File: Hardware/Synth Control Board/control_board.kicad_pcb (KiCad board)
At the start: 2 copper layers, 127 x 177.8 mm, 59 parts, among them J1 Conn_01x13, J10 Conn_01x05, J11 Conn_01x08, J12 Conn_01x06, J2 Conn_01x03, J3 Conn_01x13, J4 Conn_01x13, J5 Conn_01x02, J6 Conn_01x13, J7 Conn_01x05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

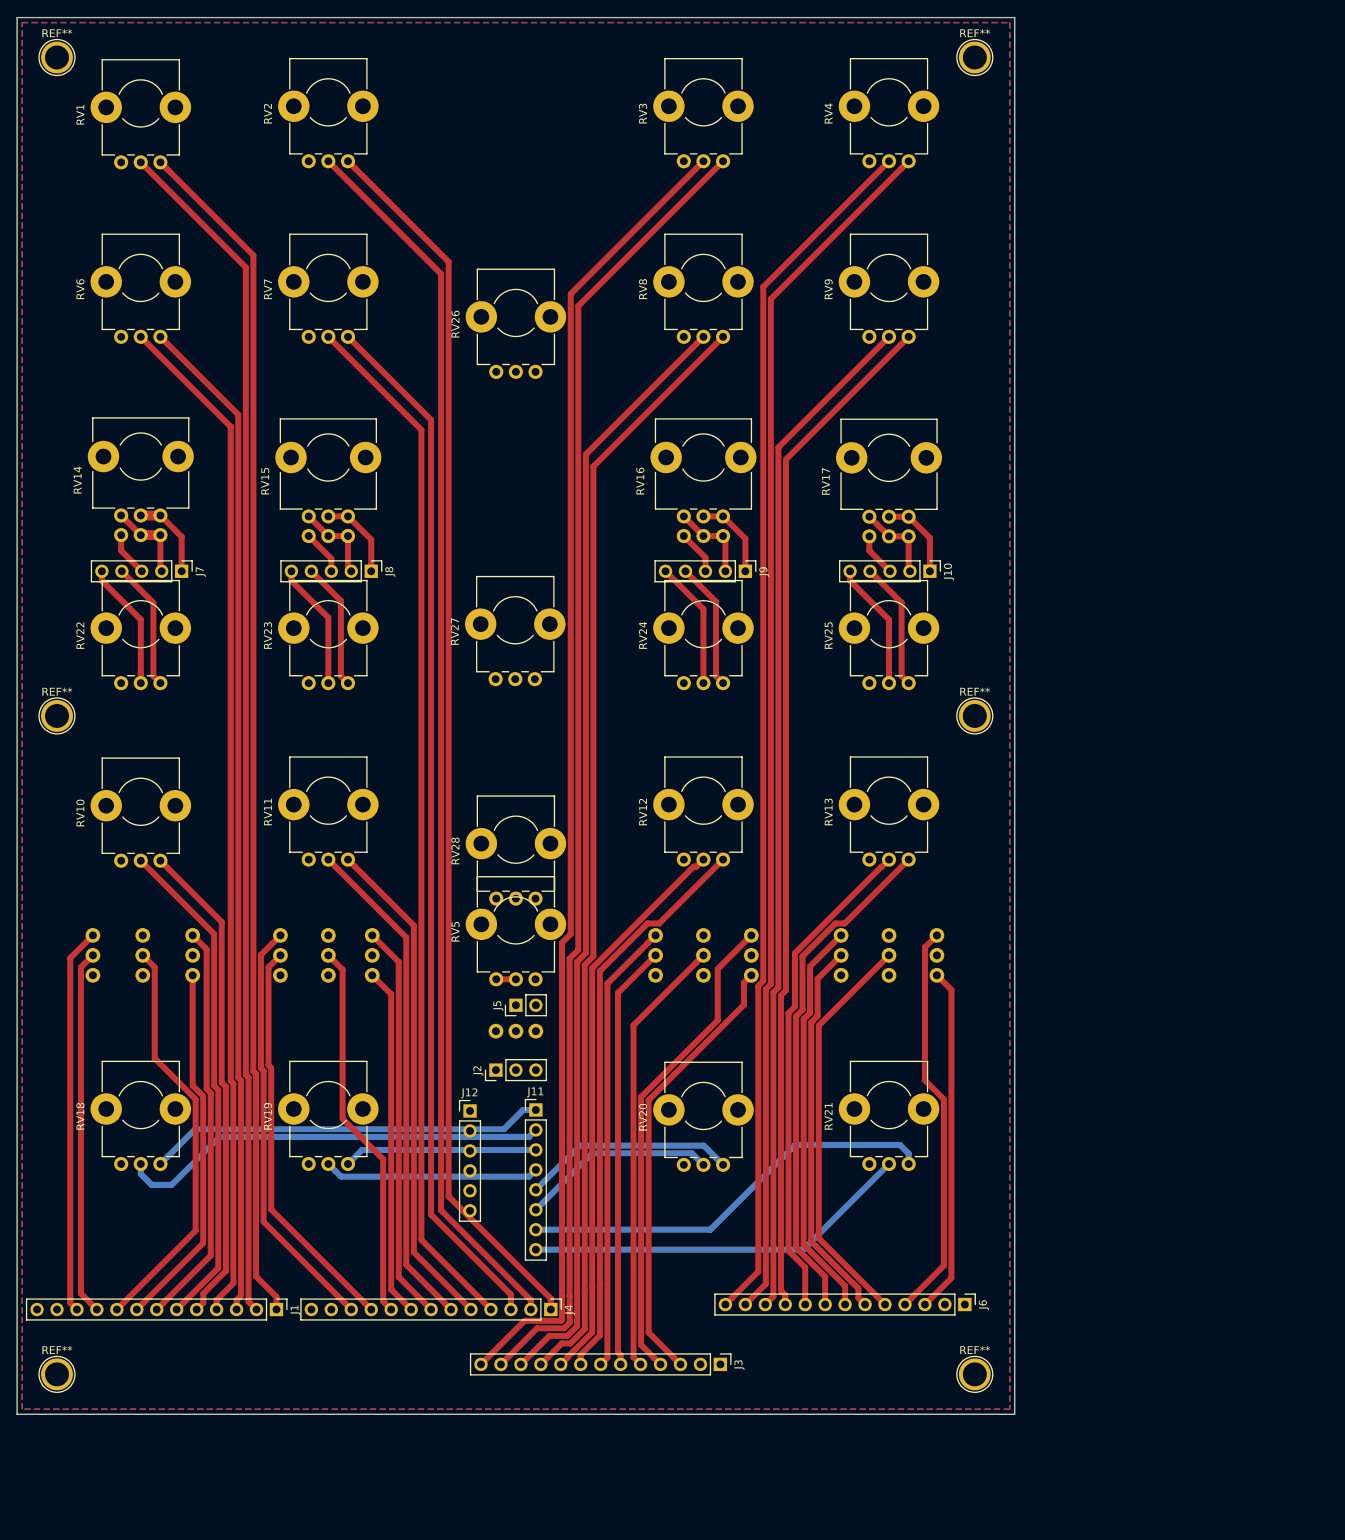
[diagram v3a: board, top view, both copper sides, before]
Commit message: redo panel layout for new enclosure. This might not be the final version, but it'll do for now.
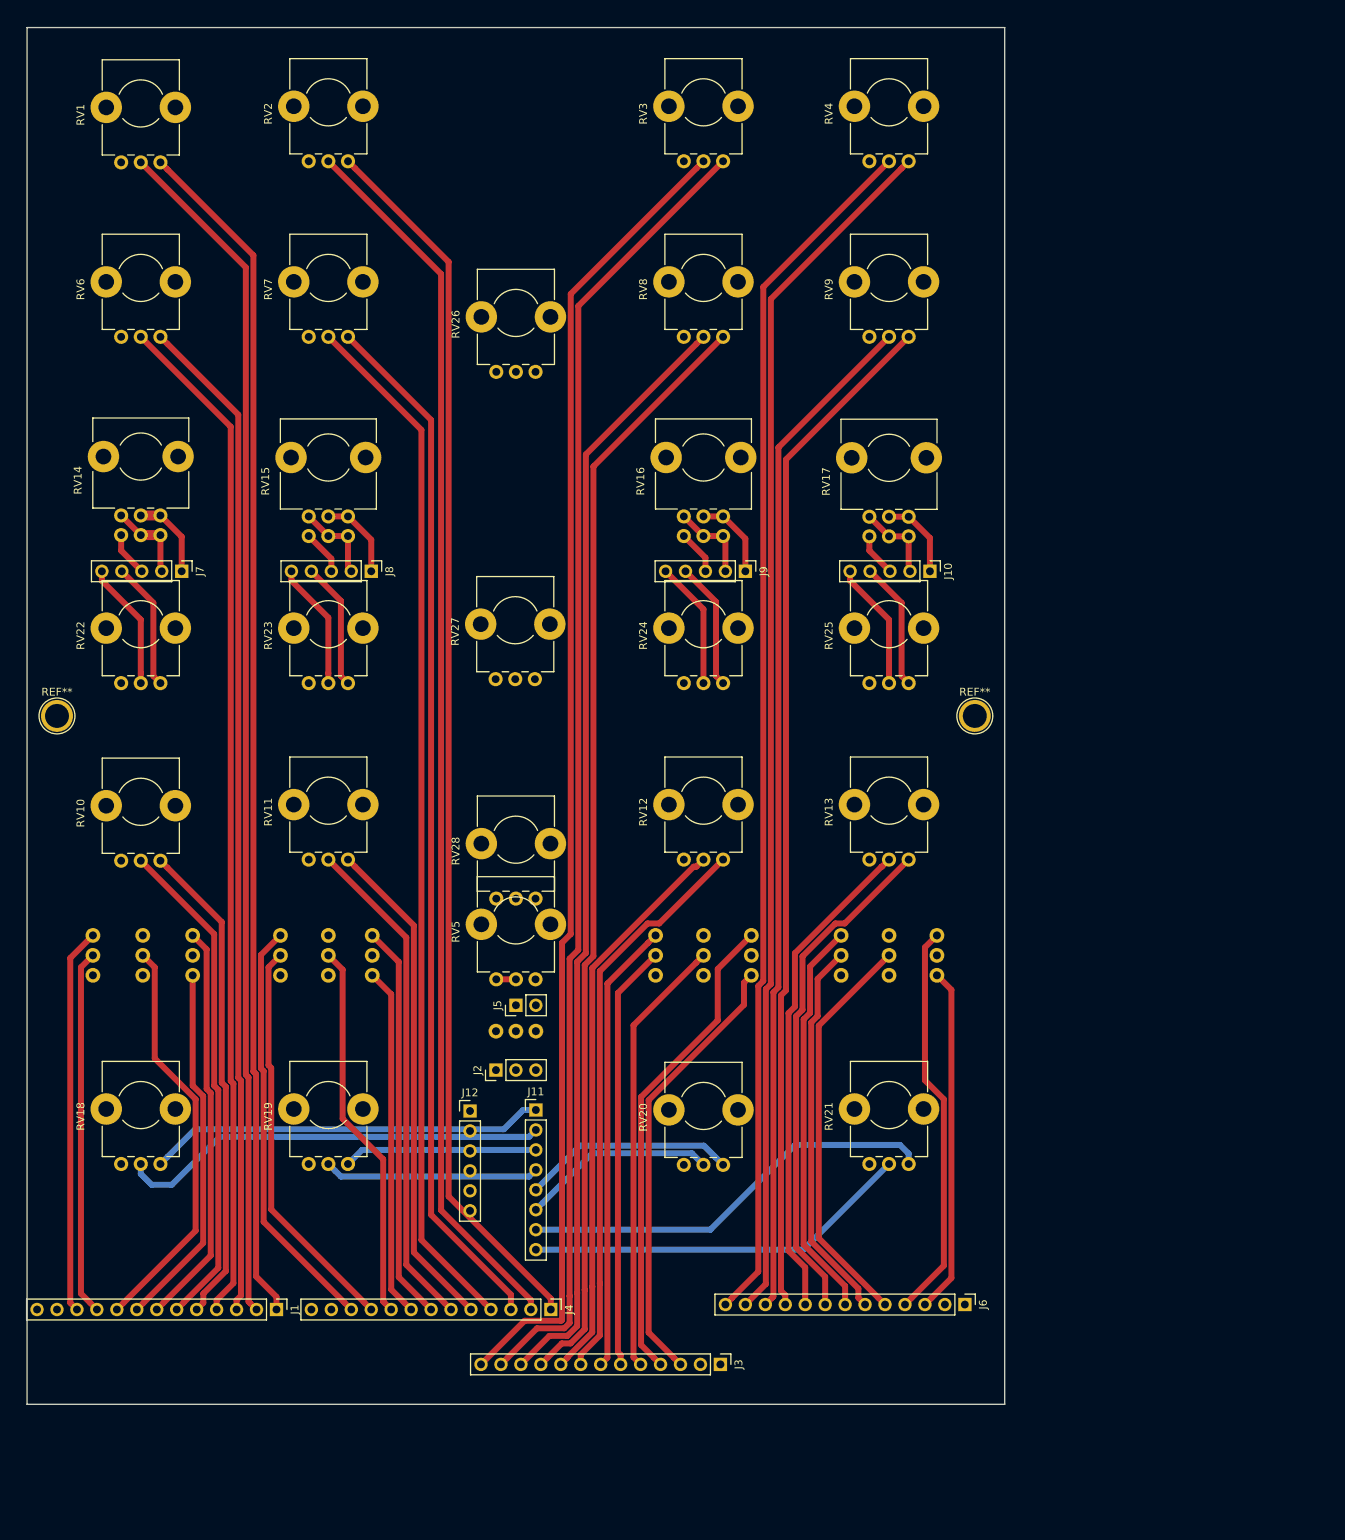
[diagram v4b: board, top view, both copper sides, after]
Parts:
- removed the REF** at (121.9, 5.08)
- removed the REF** at (5.08, 5.08)
- removed the REF** at (121.9, 172.7)
- removed the REF** at (5.08, 172.7)
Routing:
- removed copper zone on B.Cu, net GND
- removed copper zone on F.Cu, net GND
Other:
- board size 127 x 177.8 mm -> 124.5 x 175.3 mm
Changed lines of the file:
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@@
 (kicad_pcb (version 4) (host pcbnew 4.0.7)
   (general
-    (links 0)
+    (links 145)
     (no_connects 22)
-    (area -0.765 -0.075001 127.075001 177.875001)
+    (area -0.765 1.194999 125.805001 176.605001)
     (thickness 1.6)
     (drawings 4)
     (tracks 366)
     (zones 0)
-    (modules 59)
+    (modules 55)
     (nets 74)
   )
@@
     (pad 1 thru_hole circle (at 0 0) (size 4.064 4.064) (drill 3.048) (layers *.Cu *.Mask))
   )
-  (module Connectors:1pin (layer F.Cu)
-    (at 121.92 5.08)
-    (descr "module 1 pin (ou trou mecanique de percage)")
-    (tags DEV)
-    (fp_text reference REF** (at 0 -3.048) (layer F.SilkS)
-      (effects (font (size 1 1) (thickness 0.15)))
-    )
-    (fp_text value 1pin (at 0 3) (layer F.Fab)
-      (effects (font (size 1 1) (thickness 0.15)))
-    )
-    (fp_circle (center 0 0) (end 2 0.8) (layer F.Fab) (width 0.1))
-    (fp_circle (center 0 0) (end 2.6 0) (layer F.CrtYd) (width 0.05))
-    (fp_circle (center 0 0) (end 0 -2.286) (layer F.SilkS) (width 0.12))
-    (pad 1 thru_hole circle (at 0 0) (size 4.064 4.064) (drill 3.048) (layers *.Cu *.Mask))
-  )
-  (module Connectors:1pin (layer F.Cu)
-    (at 5.08 5.08)
-    (descr "module 1 pin (ou trou mecanique de percage)")
-    (tags DEV)
-    (fp_text reference REF** (at 0 -3.048) (layer F.SilkS)
-      (effects (font (size 1 1) (thickness 0.15)))
-    )
-    (fp_text value 1pin (at 0 3) (layer F.Fab)
-      (effects (font (size 1 1) (thickness 0.15)))
-    )
-    (fp_circle (center 0 0) (end 2 0.8) (layer F.Fab) (width 0.1))
-    (fp_circle (center 0 0) (end 2.6 0) (layer F.CrtYd) (width 0.05))
-    (fp_circle (center 0 0) (end 0 -2.286) (layer F.SilkS) (width 0.12))
-    (pad 1 thru_hole circle (at 0 0) (size 4.064 4.064) (drill 3.048) (layers *.Cu *.Mask))
-  )
-  (module Connectors:1pin (layer F.Cu)
-    (at 121.92 172.72)
-    (descr "module 1 pin (ou trou mecanique de percage)")
-    (tags DEV)
-    (fp_text reference REF** (at 0 -3.048) (layer F.SilkS)
-      (effects (font (size 1 1) (thickness 0.15)))
-    )
-    (fp_text value 1pin (at 0 3) (layer F.Fab)
-      (effects (font (size 1 1) (thickness 0.15)))
-    )
-    (fp_circle (center 0 0) (end 2 0.8) (layer F.Fab) (width 0.1))
-    (fp_circle (center 0 0) (end 2.6 0) (layer F.CrtYd) (width 0.05))
-    (fp_circle (center 0 0) (end 0 -2.286) (layer F.SilkS) (width 0.12))
-    (pad 1 thru_hole circle (at 0 0) (size 4.064 4.064) (drill 3.048) (layers *.Cu *.Mask))
-  )
   (module Potentiometers:Potentiometer_Bourns_PTV09A-1_Horizontal (layer F.Cu)
     (at 18.248 107.33 90)
@@
     )
   )
-  (module Connectors:1pin (layer F.Cu)
-    (at 5.08 172.72)
-    (descr "module 1 pin (ou trou mecanique de percage)")
-    (tags DEV)
-    (fp_text reference REF** (at 0 -3.048) (layer F.SilkS)
-      (effects (font (size 1 1) (thickness 0.15)))
-    )
-    (fp_text value 1pin (at 0 3) (layer F.Fab)
-      (effects (font (size 1 1) (thickness 0.15)))
-    )
-    (fp_circle (center 0 0) (end 2 0.8) (layer F.Fab) (width 0.1))
-    (fp_circle (center 0 0) (end 2.6 0) (layer F.CrtYd) (width 0.05))
-    (fp_circle (center 0 0) (end 0 -2.286) (layer F.SilkS) (width 0.12))
-    (pad 1 thru_hole circle (at 0 0) (size 4.064 4.064) (drill 3.048) (layers *.Cu *.Mask))
-  )
-  (gr_line (start 127 0) (end 0 0) (layer Edge.Cuts) (width 0.15))
-  (gr_line (start 127 177.8) (end 127 0) (layer Edge.Cuts) (width 0.15))
-  (gr_line (start 0 177.8) (end 127 177.8) (layer Edge.Cuts) (width 0.15))
-  (gr_line (start 0 0.0635) (end 0 177.8) (layer Edge.Cuts) (width 0.15))
+  (gr_line (start 1.27 176.53) (end 1.27 1.27) (layer Edge.Cuts) (width 0.15))
+  (gr_line (start 125.73 176.53) (end 1.27 176.53) (layer Edge.Cuts) (width 0.15))
+  (gr_line (start 125.73 1.27) (end 125.73 176.53) (layer Edge.Cuts) (width 0.15))
+  (gr_line (start 1.27 1.27) (end 125.73 1.27) (layer Edge.Cuts) (width 0.15))
   (segment (start 50.511033 157.191033) (end 50.511033 115.575033) (width 0.762) (layer F.Cu) (net 1))
   (segment (start 50.511033 115.575033) (end 43.023999 108.087999) (width 0.762) (layer F.Cu) (net 1))
@@
   (segment (start 51.855001 163.615001) (end 52.705 164.465) (width 0.762) (layer F.Cu) (net 67))
   (segment (start 48.587011 160.347011) (end 51.855001 163.615001) (width 0.762) (layer F.Cu) (net 67))
-  (zone (net 12) (net_name GND) (layer F.Cu) (hatch edge 0.508)
-    (connect_pads (clearance 0.508))
-    (min_thickness 0.254)
-    (fill yes (arc_segments 16) (thermal_gap 0.508) (thermal_bridge_width 0.508))
-    (polygon
-      (pts
-        (xy 0.635 0.635) (xy 126.365 0.635) (xy 126.365 177.165) (xy 0.635 177.165)
-      )
-    )
-  )
-  (zone (net 12) (net_name GND) (layer B.Cu) (hatch edge 0.508)
-    (connect_pads (clearance 0.508))
-    (min_thickness 0.254)
-    (fill yes (arc_segments 16) (thermal_gap 0.508) (thermal_bridge_width 0.508))
-    (polygon
-      (pts
-        (xy 0.635 0.635) (xy 126.365 0.635) (xy 126.365 177.165) (xy 0.635 177.165)
-      )
-    )
-  )
 )

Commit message: update control board with new pot placement from panel update
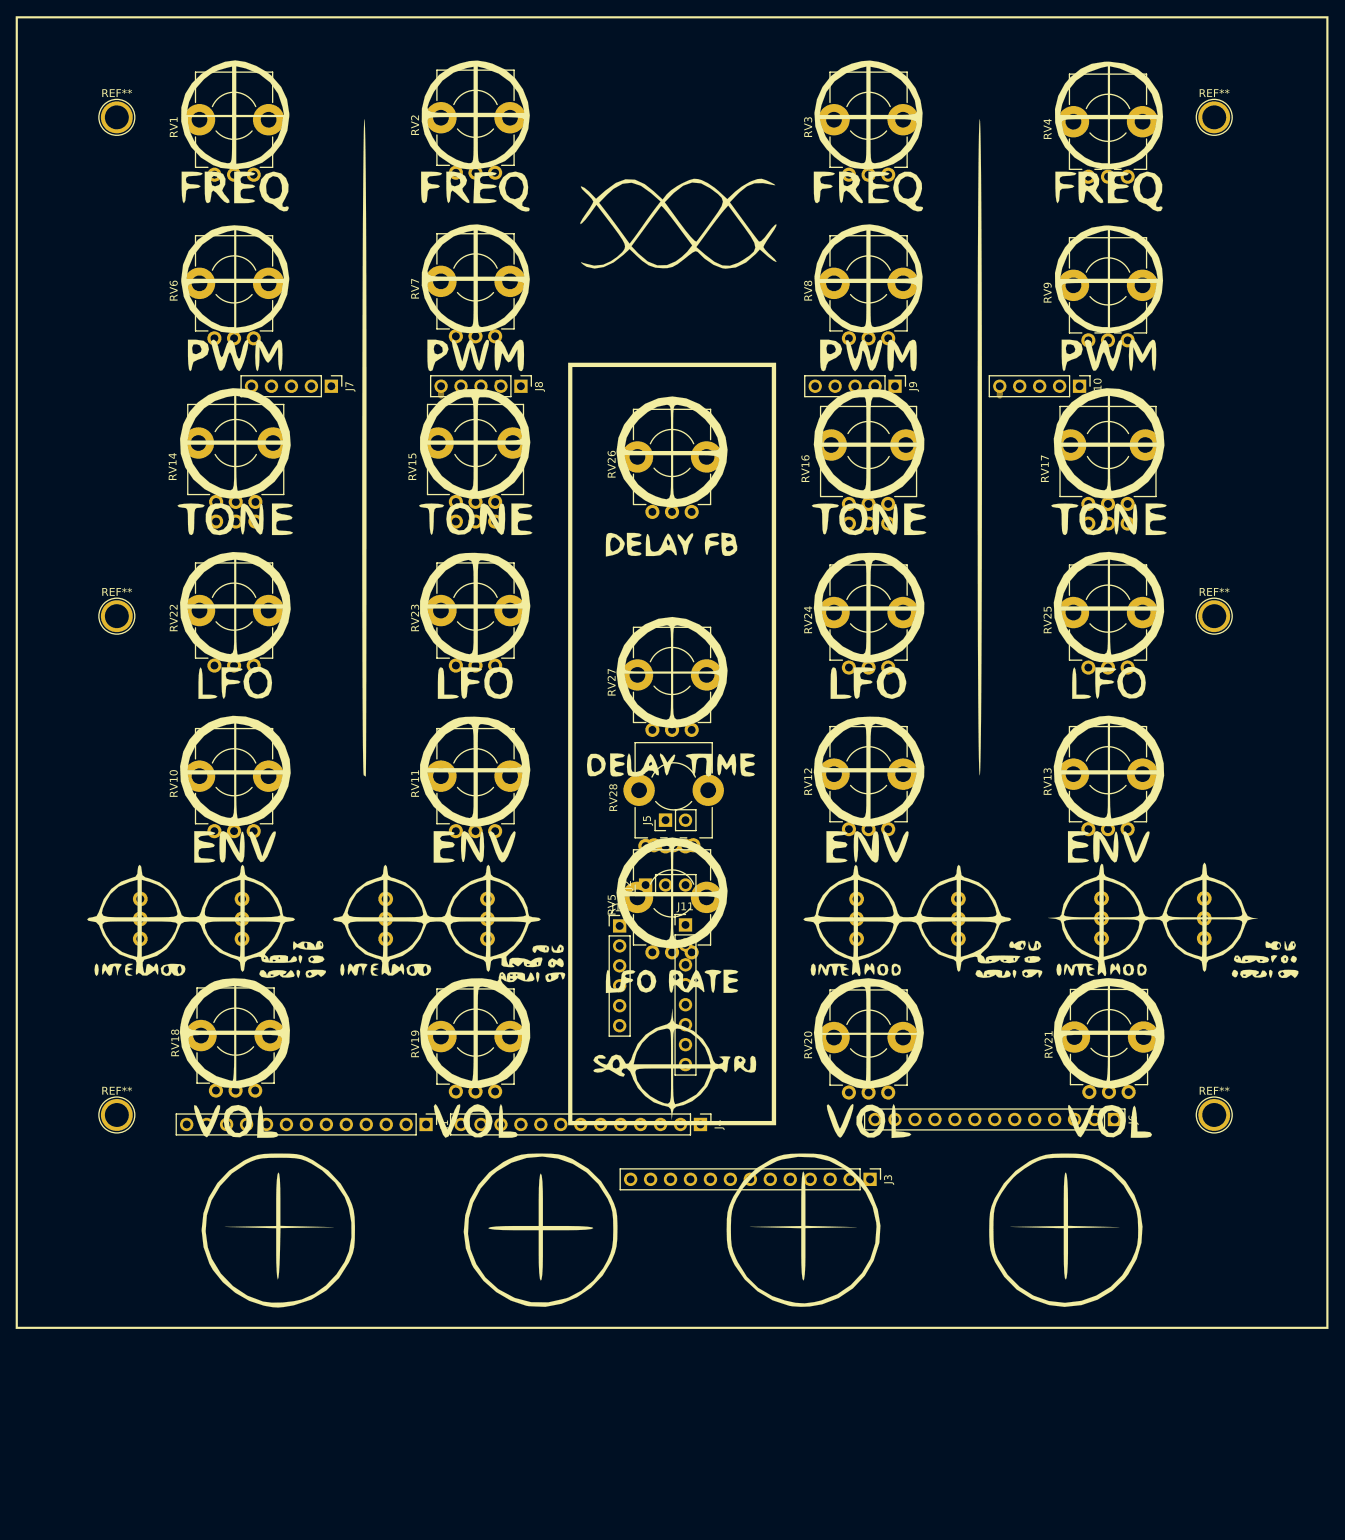
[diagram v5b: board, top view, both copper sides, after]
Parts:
- removed the REF** at (5.08, 88.9)
- removed SW10, SW11, SW12, SW13: SW_SPST, SparkFun-Electromechanical:SWITCH-SPDT
- added G***: LOGO, Panel Artwork:panel_silkscreen, F.Cu at (83.2, 83.2)
- added REF**: 1pin, Connectors:1pin, F.Cu at (152.4, 139.7)
- added REF**: 1pin, Connectors:1pin, F.Cu at (152.4, 76.2)
- added REF**: 1pin, Connectors:1pin, F.Cu at (152.4, 12.7)
- added REF**: 1pin, Connectors:1pin, F.Cu at (12.7, 76.2)
- added REF**: 1pin, Connectors:1pin, F.Cu at (12.7, 139.7)
- moved REF** 133.2 mm to (12.7, 12.7)
- moved SW6 34.4 mm to (151.1, 114.7)
- moved SW5 33.5 mm to (138.0, 114.7)
- moved J4 30.3 mm to (87.0, 140.9)
- moved J2 30.3 mm to (80.0, 110.4)
- moved J7 30.3 mm to (40.0, 46.9)
- moved J8 30.3 mm to (64.1, 46.9)
- moved J9 30.3 mm to (111.8, 46.9)
- moved J1 30.3 mm to (52.1, 140.9)
- moved J12 30.3 mm to (76.7, 115.6)
- moved J5 30.3 mm to (82.5, 102.2)
- moved SW1 30.3 mm to (82.5, 105.5)
- moved J10 30.3 mm to (135.3, 46.9)
- moved J6 30.3 mm to (139.7, 140.3)
- moved J11 30.3 mm to (85.1, 115.5)
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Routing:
- net +5V: track 1425.4 -> 0.00 mm
- net /osc3_freq_wiper: track 167.6 -> 0.00 mm
- net /osc2_freq_wiper: track 156.9 -> 0.00 mm
- net /osc4_freq_wiper: track 154.2 -> 0.00 mm
- net /osc1_freq_wiper: track 152.1 -> 0.00 mm
- net /osc3_pwm_wiper: track 141.8 -> 0.00 mm
- net /osc2_pwm_wiper: track 132.4 -> 0.00 mm
- net /osc4_pwm_wiper: track 129.7 -> 0.00 mm
- net /osc1_pwm_wiper: track 129.6 -> 0.00 mm
- net /osc3_speed: track 72.0 -> 0.00 mm
- net /osc2_speed: track 63.7 -> 0.00 mm
- net /osc1_speed: track 63.4 -> 0.00 mm
- net /osc4_speed: track 62.9 -> 0.00 mm
- net /osc3_hold: track 61.5 -> 0.00 mm
- net /envelope_pwm_bypass_in_3: track 57.5 -> 0.00 mm
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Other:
- board outline removed
